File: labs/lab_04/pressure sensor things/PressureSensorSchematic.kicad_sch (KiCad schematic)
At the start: 7 parts, among them U1 MCP601-xSN

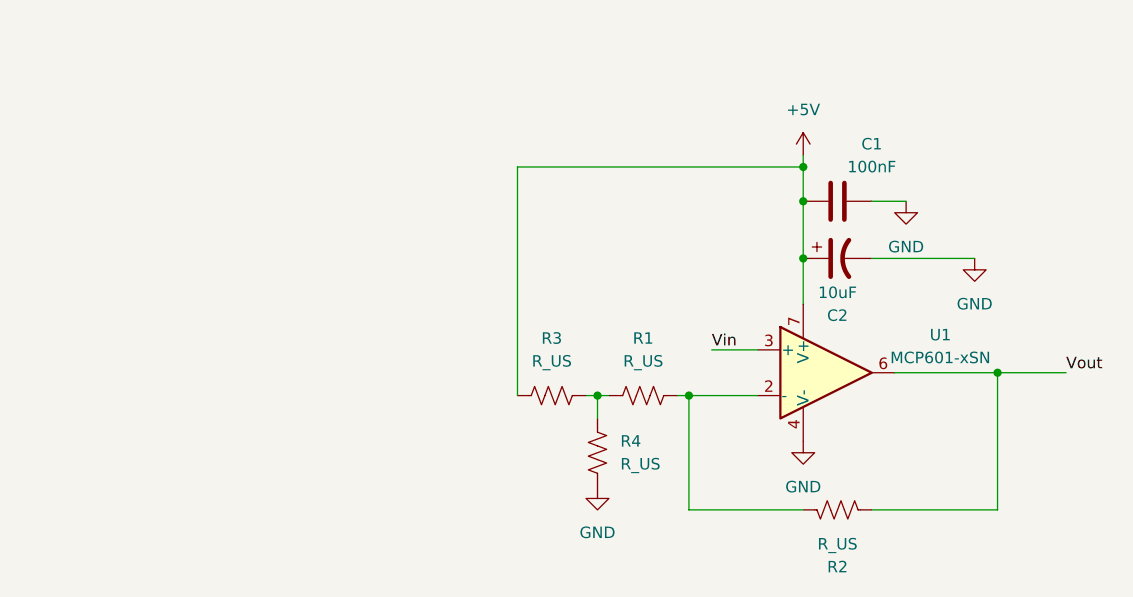
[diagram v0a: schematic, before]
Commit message: Added schematics for pressure sensor
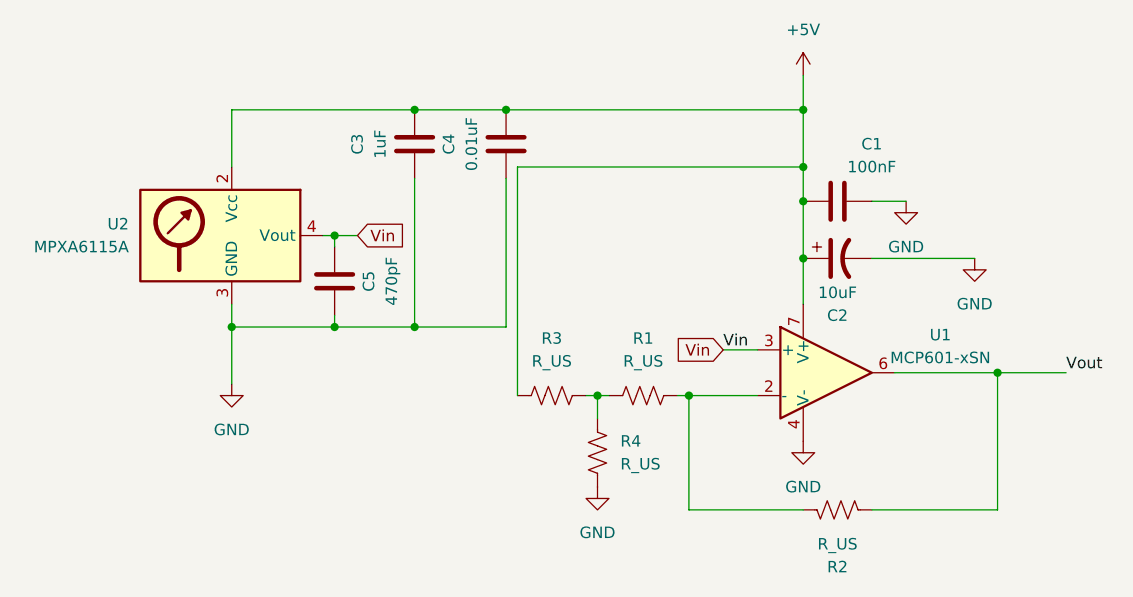
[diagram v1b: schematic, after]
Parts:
- added C3: 1uF, symbol Device:C
- added C4: 0.01uF, symbol Device:C
- added C5: 470pF, symbol Device:C
- added U2: MPXA6115A, symbol Sensor_Pressure:MPXA6115A
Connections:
- net +5V: now also C3.2, C4.2, U2.2 (Vcc)
- net GND: now also C3.1, C4.1, C5.1, U2.3 (GND)
- net Vin: now also C5.2, U2.4 (Vout)
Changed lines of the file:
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@@
   (junction (at 132.08 77.47) (diameter 0) (color 0 0 0 0)
   )
+  (junction (at 68.58 91.44) (diameter 0) (color 0 0 0 0)
+  )
+  (junction (at 88.9 91.44) (diameter 0) (color 0 0 0 0)
+  )
   (junction (at 119.38 99.06) (diameter 0) (color 0 0 0 0)
   )
+  (junction (at 80.01 81.28) (diameter 0) (color 0 0 0 0)
+  )
   (junction (at 132.08 73.66) (diameter 0) (color 0 0 0 0)
   )
+  (junction (at 88.9 67.31) (diameter 0) (color 0 0 0 0)
+  )
+  (junction (at 80.01 91.44) (diameter 0) (color 0 0 0 0)
+  )
+  (junction (at 132.08 67.31) (diameter 0) (color 0 0 0 0)
+  )
   (junction (at 132.08 83.82) (diameter 0) (color 0 0 0 0)
   )
   (junction (at 153.67 96.52) (diameter 0) (color 0 0 0 0)
   )
+  (junction (at 99.06 67.31) (diameter 0) (color 0 0 0 0)
+  )
   (wire (pts (xy 119.38 111.76) (xy 119.38 99.06))
     (stroke (width 0) (type default))
@@
     (stroke (width 0) (type default))
   )
+  (wire (pts (xy 80.01 90.17) (xy 80.01 91.44))
+    (stroke (width 0) (type default))
+  )
+  (wire (pts (xy 99.06 74.93) (xy 99.06 91.44))
+    (stroke (width 0) (type default))
+  )
+  (wire (pts (xy 80.01 82.55) (xy 80.01 81.28))
+    (stroke (width 0) (type default))
+  )
   (wire (pts (xy 153.67 96.52) (xy 153.67 111.76))
     (stroke (width 0) (type default))
   )
+  (wire (pts (xy 132.08 67.31) (xy 132.08 73.66))
+    (stroke (width 0) (type default))
+  )
   (wire (pts (xy 132.08 77.47) (xy 132.08 83.82))
     (stroke (width 0) (type default))
   )
-  (wire (pts (xy 121.92 93.98) (xy 127 93.98))
+  (wire (pts (xy 123.19 93.98) (xy 127 93.98))
+    (stroke (width 0) (type default))
+  )
+  (wire (pts (xy 68.58 97.79) (xy 68.58 91.44))
+    (stroke (width 0) (type default))
+  )
+  (wire (pts (xy 68.58 91.44) (xy 68.58 88.9))
     (stroke (width 0) (type default))
   )
@@
     (stroke (width 0) (type default))
   )
+  (wire (pts (xy 88.9 67.31) (xy 99.06 67.31))
+    (stroke (width 0) (type default))
+  )
+  (wire (pts (xy 132.08 67.31) (xy 99.06 67.31))
+    (stroke (width 0) (type default))
+  )
   (wire (pts (xy 132.08 73.66) (xy 132.08 77.47))
     (stroke (width 0) (type default))
   )
+  (wire (pts (xy 88.9 91.44) (xy 80.01 91.44))
+    (stroke (width 0) (type default))
+  )
+  (wire (pts (xy 80.01 81.28) (xy 82.55 81.28))
+    (stroke (width 0) (type default))
+  )
   (wire (pts (xy 132.08 83.82) (xy 132.08 88.9))
     (stroke (width 0) (type default))
@@
     (stroke (width 0) (type default))
   )
+  (wire (pts (xy 80.01 91.44) (xy 68.58 91.44))
+    (stroke (width 0) (type default))
+  )
   (wire (pts (xy 151.13 83.82) (xy 139.7 83.82))
     (stroke (width 0) (type default))
@@
     (stroke (width 0) (type default))
   )
+  (wire (pts (xy 99.06 91.44) (xy 88.9 91.44))
+    (stroke (width 0) (type default))
+  )
+  (wire (pts (xy 88.9 74.93) (xy 88.9 91.44))
+    (stroke (width 0) (type default))
+  )
   (wire (pts (xy 142.24 96.52) (xy 153.67 96.52))
     (stroke (width 0) (type default))
   )
-  (wire (pts (xy 132.08 72.39) (xy 132.08 73.66))
-    (stroke (width 0) (type default))
-  )
-  (label "Vin" (at 121.92 93.98 0) (fields_autoplaced)
+  (wire (pts (xy 68.58 67.31) (xy 68.58 73.66))
+    (stroke (width 0) (type default))
+  )
+  (wire (pts (xy 132.08 63.5) (xy 132.08 67.31))
+    (stroke (width 0) (type default))
+  )
+  (wire (pts (xy 88.9 67.31) (xy 68.58 67.31))
+    (stroke (width 0) (type default))
+  )
+  (wire (pts (xy 80.01 81.28) (xy 78.74 81.28))
+    (stroke (width 0) (type default))
+  )
+  (label "Vin" (at 123.19 93.98 0) (fields_autoplaced)
     (effects (font (size 1.27 1.27)) (justify left bottom))
   )
@@
     (effects (font (size 1.27 1.27)) (justify left bottom))
   )
+  (global_label "Vin" (shape input) (at 82.55 81.28 0) (fields_autoplaced)
+    (effects (font (size 1.27 1.27)) (justify left))
+    (property "Intersheetrefs" "${INTERSHEET_REFS}" (at 88.3776 81.28 0)
+      (effects (font (size 1.27 1.27)) (justify left) hide)
+    )
+  )
+  (global_label "Vin" (shape input) (at 123.19 93.98 180) (fields_autoplaced)
+    (effects (font (size 1.27 1.27)) (justify right))
+    (property "Intersheetrefs" "${INTERSHEET_REFS}" (at 117.3624 93.98 0)
+      (effects (font (size 1.27 1.27)) (justify right) hide)
+    )
+  )
   (symbol (lib_id "Device:C") (at 135.89 77.47 90) (unit 1)
     (in_bom yes) (on_board yes) (dnp no)
@@
     )
   )
-  (symbol (lib_id "power:+5V") (at 132.08 72.39 0) (unit 1)
-    (in_bom yes) (on_board yes) (dnp no) (fields_autoplaced)
-    (property "Reference" "#PWR02" (at 132.08 76.2 0)
-      (effects (font (size 1.27 1.27)) hide)
-    )
-    (property "Value" "+5V" (at 132.08 67.31 0)
-      (effects (font (size 1.27 1.27)))
-    )
-    (property "Footprint" "" (at 132.08 72.39 0)
-      (effects (font (size 1.27 1.27)) hide)
-    )
-    (property "Datasheet" "" (at 132.08 72.39 0)
+  (symbol (lib_id "power:+5V") (at 132.08 63.5 0) (unit 1)
+    (in_bom yes) (on_board yes) (dnp no) (fields_autoplaced)
+    (property "Reference" "#PWR02" (at 132.08 67.31 0)
+      (effects (font (size 1.27 1.27)) hide)
+    )
+    (property "Value" "+5V" (at 132.08 58.42 0)
+      (effects (font (size 1.27 1.27)))
+    )
+    (property "Footprint" "" (at 132.08 63.5 0)
+      (effects (font (size 1.27 1.27)) hide)
+    )
+    (property "Datasheet" "" (at 132.08 63.5 0)
       (effects (font (size 1.27 1.27)) hide)
     )
@@
     )
   )
+  (symbol (lib_id "Device:C") (at 80.01 86.36 180) (unit 1)
+    (in_bom yes) (on_board yes) (dnp no)
+    (property "Reference" "C5" (at 83.82 86.36 90)
+      (effects (font (size 1.27 1.27)))
+    )
+    (property "Value" "470pF" (at 86.36 86.36 90)
+      (effects (font (size 1.27 1.27)))
+    )
+    (property "Footprint" "" (at 79.0448 82.55 0)
+      (effects (font (size 1.27 1.27)) hide)
+    )
+    (property "Datasheet" "~" (at 80.01 86.36 0)
+      (effects (font (size 1.27 1.27)) hide)
+    )
+    (pin "1")
+    (pin "2")
+    (instances
+      (project "PressureSensorSchematic"
+        (path "/ddce9496-80ca-47e8-b333-697519785c02"
+          (reference "C5") (unit 1)
+        )
+      )
+    )
+  )
   (symbol (lib_id "power:GND") (at 132.08 104.14 0) (unit 1)
     (in_bom yes) (on_board yes) (dnp no) (fields_autoplaced)
@@
         (path "/ddce9496-80ca-47e8-b333-697519785c02"
           (reference "R3") (unit 1)
+        )
+      )
+    )
+  )
+  (symbol (lib_id "Device:C") (at 88.9 71.12 180) (unit 1)
+    (in_bom yes) (on_board yes) (dnp no)
+    (property "Reference" "C3" (at 82.55 71.12 90)
+      (effects (font (size 1.27 1.27)))
+    )
+    (property "Value" "1uF" (at 85.09 71.12 90)
+      (effects (font (size 1.27 1.27)))
+    )
+    (property "Footprint" "" (at 87.9348 67.31 0)
+      (effects (font (size 1.27 1.27)) hide)
+    )
+    (property "Datasheet" "~" (at 88.9 71.12 0)
+      (effects (font (size 1.27 1.27)) hide)
+    )
+    (pin "1")
+    (pin "2")
+    (instances
+      (project "PressureSensorSchematic"
+        (path "/ddce9496-80ca-47e8-b333-697519785c02"
+          (reference "C3") (unit 1)
+        )
+      )
+    )
+  )
+  (symbol (lib_id "power:GND") (at 68.58 97.79 0) (unit 1)
+    (in_bom yes) (on_board yes) (dnp no) (fields_autoplaced)
+    (property "Reference" "#PWR06" (at 68.58 104.14 0)
+      (effects (font (size 1.27 1.27)) hide)
+    )
+    (property "Value" "GND" (at 68.58 102.87 0)
+      (effects (font (size 1.27 1.27)))
+    )
+    (property "Footprint" "" (at 68.58 97.79 0)
+      (effects (font (size 1.27 1.27)) hide)
+    )
+    (property "Datasheet" "" (at 68.58 97.79 0)
+      (effects (font (size 1.27 1.27)) hide)
+    )
+    (pin "1")
+    (instances
+      (project "PressureSensorSchematic"
+        (path "/ddce9496-80ca-47e8-b333-697519785c02"
+          (reference "#PWR06") (unit 1)
+        )
+      )
+    )
+  )
+  (symbol (lib_id "Device:C") (at 99.06 71.12 180) (unit 1)
+    (in_bom yes) (on_board yes) (dnp no)
+    (property "Reference" "C4" (at 92.71 71.12 90)
+      (effects (font (size 1.27 1.27)))
+    )
+    (property "Value" "0.01uF" (at 95.25 71.12 90)
+      (effects (font (size 1.27 1.27)))
+    )
+    (property "Footprint" "" (at 98.0948 67.31 0)
+      (effects (font (size 1.27 1.27)) hide)
+    )
+    (property "Datasheet" "~" (at 99.06 71.12 0)
+      (effects (font (size 1.27 1.27)) hide)
+    )
+    (pin "1")
+    (pin "2")
+    (instances
+      (project "PressureSensorSchematic"
+        (path "/ddce9496-80ca-47e8-b333-697519785c02"
+          (reference "C4") (unit 1)
         )
       )
@@
         )
       )
+    )
+  )
+  (symbol (lib_id "Sensor_Pressure:MPXA6115A") (at 68.58 81.28 0) (unit 1)
+    (in_bom yes) (on_board yes) (dnp no) (fields_autoplaced)
+    (property "Reference" "U2" (at 57.15 80.01 0)
+      (effects (font (size 1.27 1.27)) (justify right))
+    )
+    (property "Value" "MPXA6115A" (at 57.15 82.55 0)
+      (effects (font (size 1.27 1.27)) (justify right))
+    )
+    (property "Footprint" "" (at 55.88 90.17 0)
+      (effects (font (size 1.27 1.27)) hide)
+    )
+    (property "Datasheet" "https://www.nxp.com/docs/en/data-sheet/MPXA6115A.pdf" (at 68.58 66.04 0)
+      (effects (font (size 1.27 1.27)) hide)
+    )
+    (pin "1")
+    (pin "3")
+    (pin "4")
+    (pin "6")
+    (pin "7")
+    (pin "5")
+    (pin "2")
+    (pin "8")
+    (instances
+      (project "PressureSensorSchematic"
+        (path "/ddce9496-80ca-47e8-b333-697519785c02"
+          (reference "U2") (unit 1)
+        )
+      )

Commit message: Resistance values in pressure sensor
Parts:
- R1: value R_US -> 110k ohms
- R2: value R_US -> 330k ohms
- R3: value R_US -> 470k ohms
- R4: value R_US -> 122k ohms
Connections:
- net +5V: now also R3.2; no longer R3.1
- net at R1.1, R4.1: now also R3.1; no longer R3.2
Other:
- moved on the sheet: R3
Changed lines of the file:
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@@
     (stroke (width 0) (type default))
   )
-  (wire (pts (xy 100.33 73.66) (xy 100.33 99.06))
+  (wire (pts (xy 109.22 73.66) (xy 109.22 91.44))
     (stroke (width 0) (type default))
   )
@@
     (stroke (width 0) (type default))
   )
-  (wire (pts (xy 132.08 73.66) (xy 100.33 73.66))
+  (wire (pts (xy 132.08 73.66) (xy 109.22 73.66))
     (stroke (width 0) (type default))
   )
   (wire (pts (xy 109.22 99.06) (xy 109.22 101.6))
-    (stroke (width 0) (type default))
-  )
-  (wire (pts (xy 107.95 99.06) (xy 109.22 99.06))
     (stroke (width 0) (type default))
   )
@@
     )
   )
-  (symbol (lib_id "Device:R_US") (at 109.22 105.41 0) (unit 1)
-    (in_bom yes) (on_board yes) (dnp no) (fields_autoplaced)
-    (property "Reference" "R4" (at 111.76 104.14 0)
+  (symbol (lib_id "Device:R_US") (at 109.22 105.41 0) (mirror y) (unit 1)
+    (in_bom yes) (on_board yes) (dnp no)
+    (property "Reference" "R4" (at 106.68 104.14 0)
       (effects (font (size 1.27 1.27)) (justify left))
     )
-    (property "Value" "R_US" (at 111.76 106.68 0)
+    (property "Value" "122k ohms" (at 106.68 106.68 0)
       (effects (font (size 1.27 1.27)) (justify left))
     )
-    (property "Footprint" "" (at 110.236 105.664 90)
+    (property "Footprint" "" (at 108.204 105.664 90)
       (effects (font (size 1.27 1.27)) hide)
     )
@@
       (effects (font (size 1.27 1.27)))
     )
-    (property "Value" "R_US" (at 135.89 115.57 90)
+    (property "Value" "330k ohms" (at 135.89 115.57 90)
       (effects (font (size 1.27 1.27)))
     )
@@
     )
   )
-  (symbol (lib_id "Device:R_US") (at 104.14 99.06 90) (unit 1)
-    (in_bom yes) (on_board yes) (dnp no) (fields_autoplaced)
-    (property "Reference" "R3" (at 104.14 92.71 90)
-      (effects (font (size 1.27 1.27)))
-    )
-    (property "Value" "R_US" (at 104.14 95.25 90)
-      (effects (font (size 1.27 1.27)))
-    )
-    (property "Footprint" "" (at 104.394 98.044 90)
-      (effects (font (size 1.27 1.27)) hide)
-    )
-    (property "Datasheet" "~" (at 104.14 99.06 0)
+  (symbol (lib_id "Device:R_US") (at 109.22 95.25 0) (mirror x) (unit 1)
+    (in_bom yes) (on_board yes) (dnp no)
+    (property "Reference" "R3" (at 106.68 93.98 0)
+      (effects (font (size 1.27 1.27)) (justify right))
+    )
+    (property "Value" "470k ohms" (at 106.68 96.52 0)
+      (effects (font (size 1.27 1.27)) (justify right))
+    )
+    (property "Footprint" "" (at 110.236 94.996 90)
+      (effects (font (size 1.27 1.27)) hide)
+    )
+    (property "Datasheet" "~" (at 109.22 95.25 0)
       (effects (font (size 1.27 1.27)) hide)
     )
@@
       (effects (font (size 1.27 1.27)))
     )
-    (property "Value" "MCP601-xSN" (at 147.32 94.8691 0)
+    (property "Value" "MCP601-xSN" (at 148.59 95.25 0)
       (effects (font (size 1.27 1.27)))
     )
@@
   )
   (symbol (lib_id "Device:R_US") (at 114.3 99.06 90) (unit 1)
-    (in_bom yes) (on_board yes) (dnp no) (fields_autoplaced)
-    (property "Reference" "R1" (at 114.3 92.71 90)
-      (effects (font (size 1.27 1.27)))
-    )
-    (property "Value" "R_US" (at 114.3 95.25 90)
-      (effects (font (size 1.27 1.27)))
-    )
+    (in_bom yes) (on_board yes) (dnp no)
+    (property "Reference" "R1" (at 114.3 93.98 90)
+      (effects (font (size 1.27 1.27)))
+    )
+    (property "Value" "110k ohms" (at 115.57 96.52 90)
+      (effects (font (size 1.27 1.27)))
+    )
